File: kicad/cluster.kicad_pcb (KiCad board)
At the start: 2 copper layers, 24.5 x 36.5 mm, 17 parts, among them J1 Conn_01x07

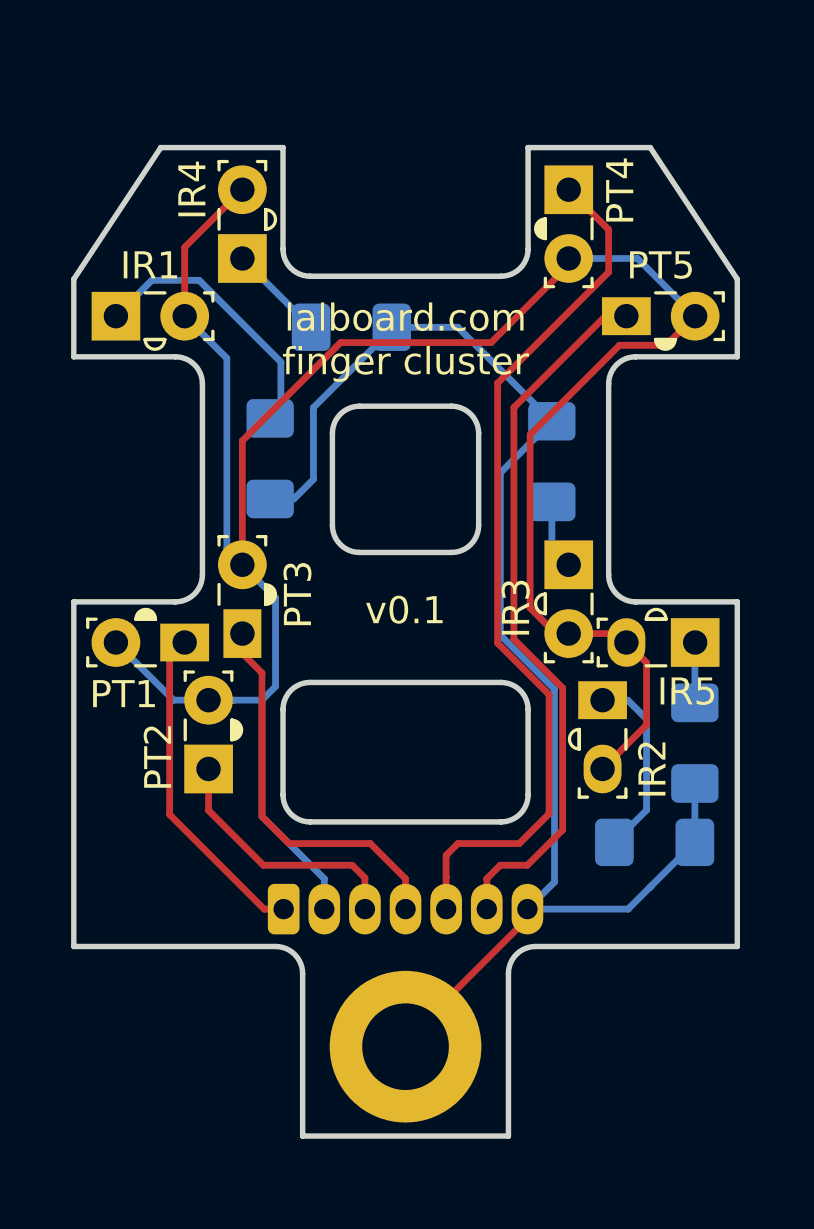
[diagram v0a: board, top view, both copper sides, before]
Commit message: Added ground planes, combined left and right thumb cluster PCBs
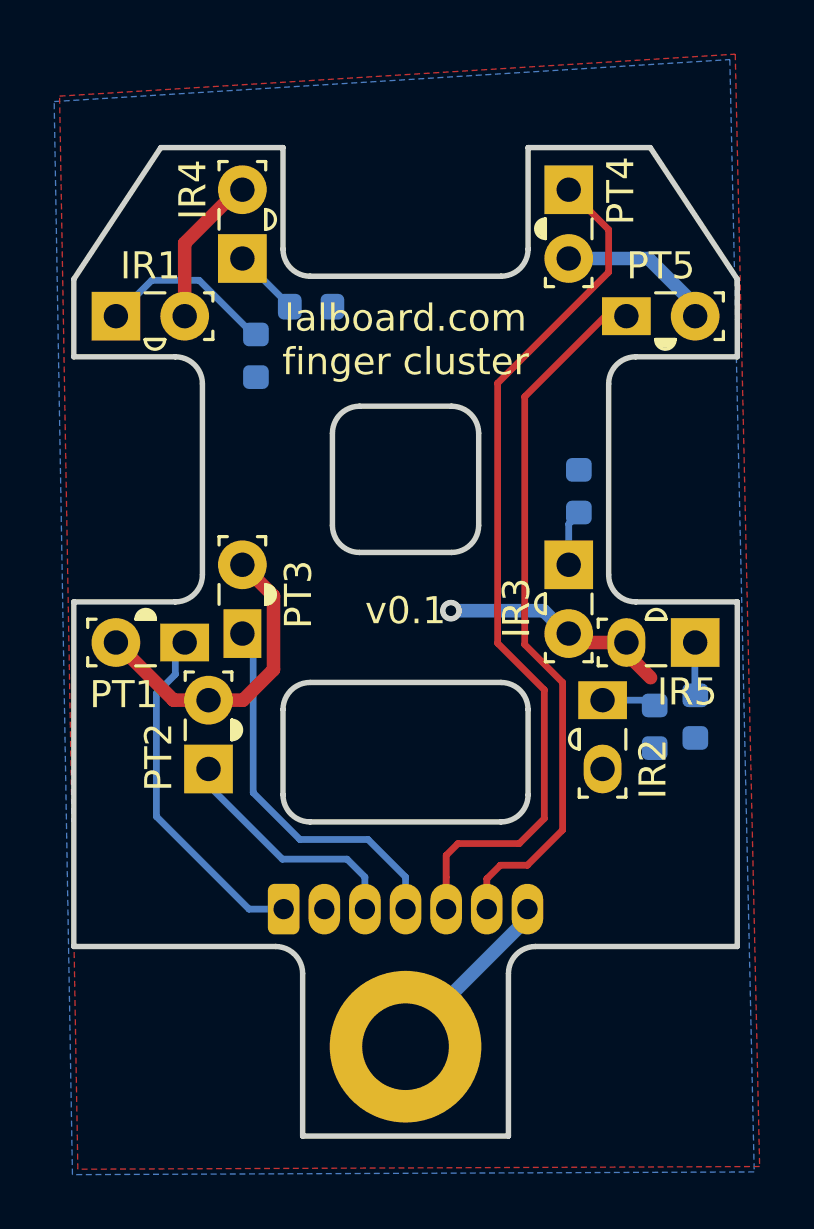
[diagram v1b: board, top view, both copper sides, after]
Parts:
- R1, R2, R3, R4, R5: footprint Resistor_SMD:R_1206_3216Metric_Pad1.42x1.75mm_HandSolder -> Resistor_SMD:R_0603_1608Metric
- moved R2 4.27 mm to (174.5, 110.2), turned to 90 degrees
- moved R1 3.84 mm to (159.8, 96.5)
- moved R4 1.67 mm to (161.8, 94.7)
- moved R3 1.48 mm to (171.7, 101.5)
- moved R5 0.98 mm to (176.0, 109.8)
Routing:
- net +5V: track 86.4 -> 31.8 mm, vias 0 -> 1
- net GND: track 52.5 -> 6.94 mm
- net Net-(IR2-Pad1): track 6.96 -> 2.13 mm
- net Net-(IR1-Pad1): track 9.97 -> 6.59 mm
- net C1: track 12.2 -> 13.8 mm
- net Net-(IR4-Pad1): track 3.59 -> 2.55 mm
- net C3: track 9.49 -> 8.97 mm
- added copper zone on F.Cu, net +5V
- added copper zone on B.Cu, net GND
